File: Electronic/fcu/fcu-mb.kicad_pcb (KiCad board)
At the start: 2 copper layers, 122 x 73.7 mm, 58 parts, among them T1 BS170

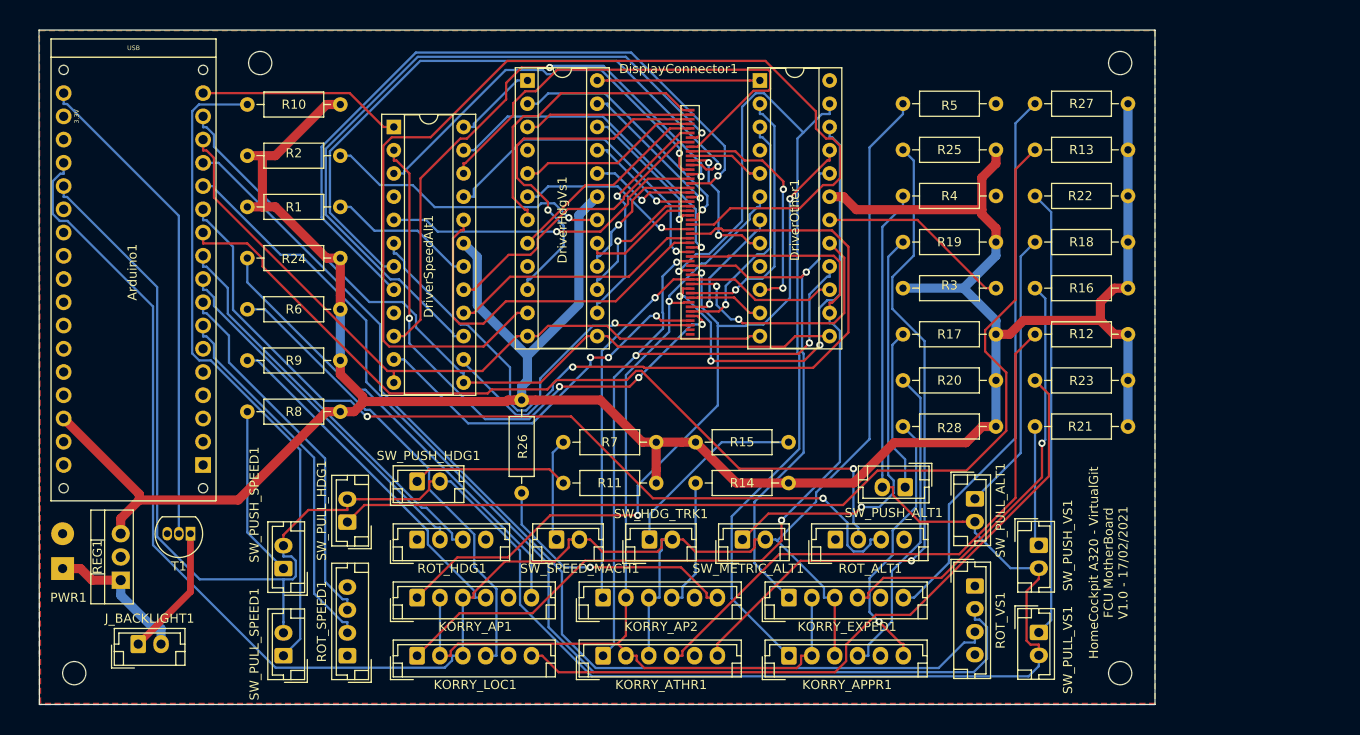
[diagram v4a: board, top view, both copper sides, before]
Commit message: Update electornic schema of FCU MotherBoard and Display. Replace MAX7219 for leds to dedicated TLC5917.
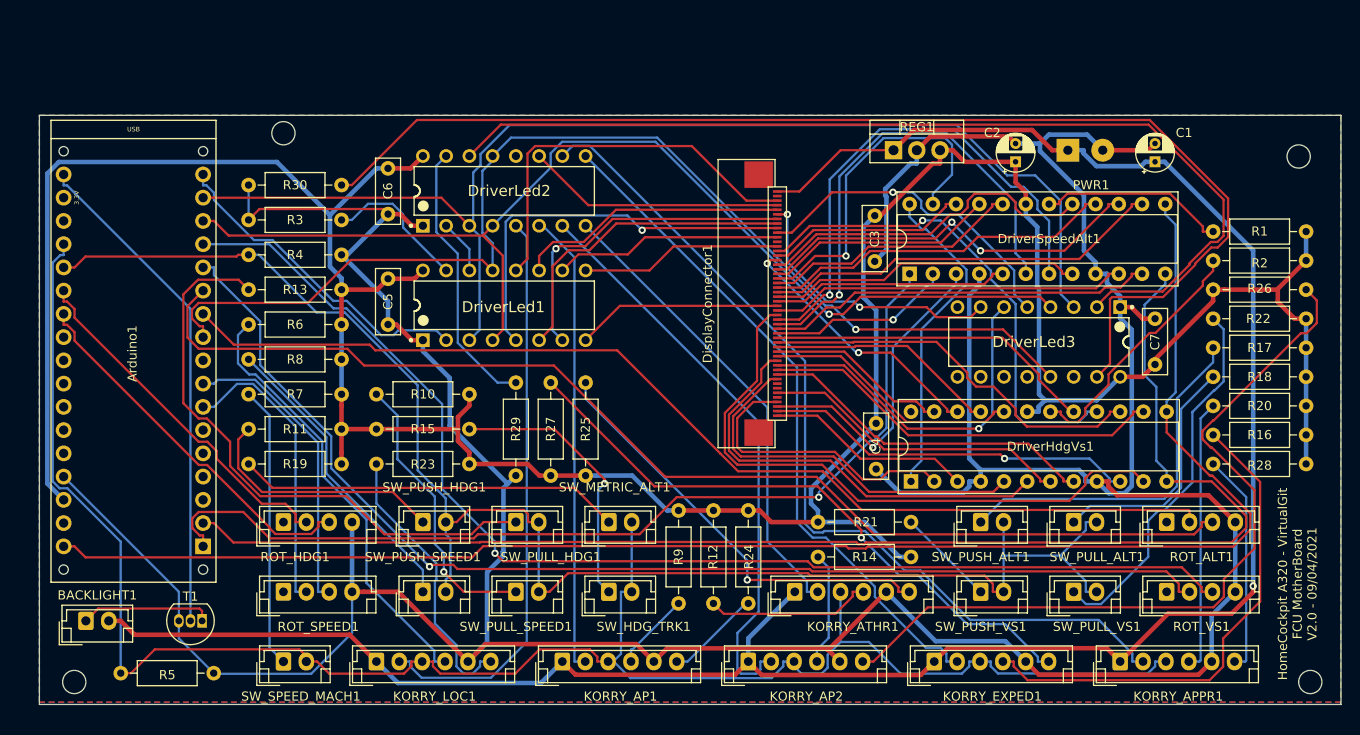
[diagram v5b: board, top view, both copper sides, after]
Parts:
- removed DriverOther1: MAX7219, Package_DIP:DIP-24_W7.62mm_Socket
- added C1: 100µF, Capacitor_THT:CP_Radial_D4.0mm_P2.00mm, F.Cu at (162.6, 88.9)
- added C2: 10µF, Capacitor_THT:CP_Radial_D4.0mm_P2.00mm, F.Cu at (147.3, 88.9)
- added C3: 0,1µF, Capacitor_THT:C_Disc_D7.0mm_W2.5mm_P5.00mm, F.Cu at (131.9, 94.8)
- added C4: 0,1µF, Capacitor_THT:C_Disc_D7.0mm_W2.5mm_P5.00mm, F.Cu at (132.1, 117.5)
- added C5: 1µF, Capacitor_THT:C_Disc_D7.0mm_W2.5mm_P5.00mm, F.Cu at (78.7, 106.7)
- added C6: 1µF, Capacitor_THT:C_Disc_D7.0mm_W2.5mm_P5.00mm, F.Cu at (78.7, 94.6)
- added C7: 1µF, Capacitor_THT:C_Disc_D7.0mm_W2.5mm_P5.00mm, F.Cu at (162.6, 106.0)
- added DriverLed1: TLC5917IN, home-cockpit-footprints:Texas_Instruments-TLC5917IN-Manufacturer_Recommended, F.Cu at (91.4, 104.6)
- added DriverLed2: TLC5917IN, home-cockpit-footprints:Texas_Instruments-TLC5917IN-Manufacturer_Recommended, F.Cu at (91.4, 92.1)
- added DriverLed3: TLC5917IN, home-cockpit-footprints:Texas_Instruments-TLC5917IN-Manufacturer_Recommended, F.Cu at (149.9, 108.6)
- added R29: 9,53kohms, Resistor_THT:R_Axial_DIN0207_L6.3mm_D2.5mm_P10.16mm_Horizontal, F.Cu at (92.7, 123.2)
- added R30: 9,53kohms, Resistor_THT:R_Axial_DIN0207_L6.3mm_D2.5mm_P10.16mm_Horizontal, F.Cu at (63.5, 91.4)
- moved PWR1 119.0 mm to (153.0, 87.6), turned to 0 degrees
- moved R2 116.3 mm to (179.1, 99.7), turned to 180 degrees
- moved R1 115.7 mm to (179.1, 96.5), turned to 180 degrees
- moved R5 105.7 mm to (59.7, 144.8)
- moved REG1 96.6 mm to (134.0, 87.6), turned to 0 degrees
- moved R26 88.6 mm to (179.1, 102.9), turned to 180 degrees
- moved R13 87.3 mm to (63.5, 102.9)
- moved R19 75.5 mm to (63.5, 121.9)
- moved R23 72.6 mm to (77.5, 121.9)
- moved R3 71.9 mm to (63.5, 95.2)
- moved R4 71.8 mm to (73.7, 99.1)
- moved R24 66.5 mm to (118.1, 137.2), turned to 90 degrees
- moved R27 61.1 mm to (96.5, 113.0), turned to 270 degrees
- moved DriverHdgVs1 60.6 mm to (135.9, 123.8), turned to 90 degrees
- moved DriverSpeedAlt1 58.6 mm to (135.7, 101.1), turned to 90 degrees
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- renumbered J_BACKLIGHT1 to BACKLIGHT1
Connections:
- Arduino1 pad A2: Net-(Arduino1-PadA2) -> ROT_HDG_A
- Arduino1 pad A3: Net-(Arduino1-PadA3) -> ROT_HDG_B
- Arduino1 pad D10: DriverLoad -> DriverLedLoad
- Arduino1 pad D11: DriverClock -> DriverLedClock
- Arduino1 pad D12: DriverData -> DriverLedData
- Arduino1 pad D4: ROT_HDG_A -> Net-(Arduino1-PadD4)
- Arduino1 pad D5: ROT_HDG_B -> LedOutputEnable
- Arduino1 pad MOSI: Net-(Arduino1-PadMOSI) -> DriverDigitData
- Arduino1 pad SCK: Net-(Arduino1-PadSCK) -> DriverDigitClock
- Arduino1 pad SS: Net-(Arduino1-PadSS) -> DriverDigitLoad
- BACKLIGHT1 pad 2: +12V -> Vcc12V
- DisplayConnector1 pad 1: hdgVsDig3 -> Vcc12V
- DisplayConnector1 pad 10: Dr3Dig5 -> LedManagedSpeed
- DisplayConnector1 pad 11: Dr3Dig6 -> LedPadVS
- DisplayConnector1 pad 12: Dr3Dig7 -> Net-(DisplayConnector1-Pad12)
- DisplayConnector1 pad 13: speedAltDig3 -> LedPadLAT
- DisplayConnector1 pad 14: speedAltDig4 -> hdgVsB
- DisplayConnector1 pad 15: speedAltDig5 -> speedAltDP
- DisplayConnector1 pad 16: speedAltDig6 -> hdgVsDP
- DisplayConnector1 pad 17: speedAltDig7 -> speedAltG
- DisplayConnector1 pad 18: hdgVsB -> speedAltF
- DisplayConnector1 pad 19: hdgVsC -> speedAltE
- DisplayConnector1 pad 2: hdgVsDig4 -> Net-(DisplayConnector1-Pad2)
- DisplayConnector1 pad 20: hdgVsD -> speedAltD
- DisplayConnector1 pad 21: hdgVsE -> speedAltC
- DisplayConnector1 pad 22: hdgVsF -> speedAltB
- DisplayConnector1 pad 23: hdgVsG -> speedAltA
- DisplayConnector1 pad 24: hdgVsDP -> speedAltDig7
- DisplayConnector1 pad 25: hdgVsDig0 -> speedAltDig6
- DisplayConnector1 pad 26: hdgVsDig1 -> LedPadTRK
- DisplayConnector1 pad 27: hdgVsDig2 -> speedAltDig5
- DisplayConnector1 pad 28: speedAltA -> hdgVsDig1
- DisplayConnector1 pad 29: speedAltB -> speedAltDig3
- DisplayConnector1 pad 3: hdgVsDig5 -> LedPadStaticALT
- DisplayConnector1 pad 30: speedAltC -> speedAltDig2
- DisplayConnector1 pad 31: speedAltD -> speedAltDig1
- DisplayConnector1 pad 32: speedAltE -> speedAltDig0
- DisplayConnector1 pad 33: Dr3SegA -> hdgVsG
- DisplayConnector1 pad 34: Dr3SegB -> hdgVsF
- DisplayConnector1 pad 35: Dr3SegC -> hdgVsE
- DisplayConnector1 pad 36: Dr3SegD -> hdgVsD
- DisplayConnector1 pad 37: Dr3SegE -> hdgVsC
- DisplayConnector1 pad 38: Dr3SegF -> hdgVsDig2
- DisplayConnector1 pad 39: Dr3SegG -> LedManagedHDG
- DisplayConnector1 pad 4: hdgVsDig6 -> LedPadStaticLines
- DisplayConnector1 pad 40: Dr3SegDP -> hdgVsA
- DisplayConnector1 pad 41: Dr3Dig0 -> hdgVsDig7
- DisplayConnector1 pad 42: Dr3Dig1 -> hdgVsDig6
- DisplayConnector1 pad 43: Dr3Dig2 -> Net-(DisplayConnector1-Pad43)
- DisplayConnector1 pad 44: Dr3Dig3 -> Net-(DisplayConnector1-Pad44)
- DisplayConnector1 pad 45: Dr3Dig4 -> hdgVsDig3
- DisplayConnector1 pad 46: speedAltDig0 -> Net-(DisplayConnector1-Pad46)
- DisplayConnector1 pad 47: speedAltDig1 -> hdgVsDig0
- DisplayConnector1 pad 48: speedAltDig2 -> speedAltDig4
- DisplayConnector1 pad 49: Net-(DisplayConnector1-Pad49) -> hdgVsDig5
- DisplayConnector1 pad 5: hdgVsDig7 -> LedPadFPA
- DisplayConnector1 pad 50: Net-(DisplayConnector1-Pad50) -> hdgVsDig4
- DisplayConnector1 pad 6: hdgVsA -> LedManagedALT
- DisplayConnector1 pad 7: speedAltF -> LedPadHDG
- DisplayConnector1 pad 8: speedAltG -> LedPadMACH
- DisplayConnector1 pad 9: speedAltDP -> LedPadSPD
- DriverHdgVs1 pad 12: DriverLoad -> DriverDigitLoad
- DriverHdgVs1 pad 13: DriverClock -> DriverDigitClock
- DriverSpeedAlt1 pad 1: DriverData -> DriverDigitData
- DriverSpeedAlt1 pad 12: DriverLoad -> DriverDigitLoad
- DriverSpeedAlt1 pad 13: DriverClock -> DriverDigitClock
- KORRY_AP1 pad 1: Dr3SegE -> Vcc12V
- KORRY_AP1 pad 2: Dr3Dig2 -> LedKorryAP1
- KORRY_AP2 pad 1: Dr3SegF -> Vcc12V
- KORRY_AP2 pad 2: Dr3Dig2 -> LedKorryAP2
- KORRY_APPR1 pad 1: Dr3SegD -> Vcc12V
- KORRY_APPR1 pad 2: Dr3Dig2 -> LedKorryAPPR
- KORRY_ATHR1 pad 1: Dr3SegB -> Vcc12V
- KORRY_ATHR1 pad 2: Dr3Dig2 -> LedKorryATHR
- KORRY_EXPED1 pad 1: Dr3SegC -> Vcc12V
- KORRY_EXPED1 pad 2: Dr3Dig2 -> LedKorryEXPED
- KORRY_LOC1 pad 1: Dr3SegA -> Vcc12V
- KORRY_LOC1 pad 2: Dr3Dig2 -> LedKorryLoc
- PWR1 pad 1: +12V -> Vcc12V
- R3 pad 1: +5V -> GND
- REG1 pad 1: +12V -> Vcc12V
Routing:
- net GND: track 0.00 -> 431.0 mm
- net Vcc12V: track 0.00 -> 243.9 mm, vias 0 -> 1
- net DriverDigitClock: track 0.00 -> 172.1 mm
- net DriverDigitLoad: track 0.00 -> 151.9 mm
- net DriverLedClock: track 0.00 -> 132.5 mm
- net Net-(DriverLed3-Pad15): track 0.00 -> 132.5 mm
- net LedOutputEnable: track 0.00 -> 125.4 mm, vias 0 -> 1
- net DriverLedLoad: track 0.00 -> 120.3 mm, vias 0 -> 1
- net Dr3Dig2: track 115.2 -> 0.00 mm, vias 1 -> 0
- net Net-(DriverLed2-Pad14): track 0.00 -> 108.4 mm
- net DriverDigitData: track 0.00 -> 104.3 mm, vias 0 -> 1
- net Dr3SegD: track 100.1 -> 0.00 mm, vias 1 -> 0
- net LedKorryAPPR: track 0.00 -> 98.3 mm
- net Dr3SegA: track 96.1 -> 0.00 mm, vias 1 -> 0
- net Dr3SegE: track 87.3 -> 0.00 mm, vias 3 -> 0
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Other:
- board size 122 x 73.7 mm -> 142.2 x 64.4 mm
- board text added: "HomeCockpit A320 - VirtualGit FCU MotherBoard V2.0 - 09/04/2021"
- board text removed: "HomeCockpit A320 - VirtualGit FCU MotherBoard V1.0 - 17/02/2021"

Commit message: Adjust resistor values for TLC5917
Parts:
- R29, R3: value 9,53kohms -> 1kohms
- R30: value 9,53kohms -> 2kohms
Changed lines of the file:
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@@
       (effects (font (size 1 1) (thickness 0.15)))
     )
-    (fp_text value 9,53kohms (at 5.08 2.37) (layer F.Fab)
+    (fp_text value 2kohms (at 5.08 2.37) (layer F.Fab)
       (effects (font (size 1 1) (thickness 0.15)))
     )
@@
       (effects (font (size 1 1) (thickness 0.15)))
     )
-    (fp_text value 9,53kohms (at 5.08 2.37 90) (layer F.Fab)
+    (fp_text value 1kohms (at 5.08 2.37 90) (layer F.Fab)
       (effects (font (size 1 1) (thickness 0.15)))
     )
@@
       (effects (font (size 1 1) (thickness 0.15)))
     )
-    (fp_text value 9,53kohms (at 5.08 2.37) (layer F.Fab)
+    (fp_text value 1kohms (at 5.08 2.37) (layer F.Fab)
       (effects (font (size 1 1) (thickness 0.15)))
     )
